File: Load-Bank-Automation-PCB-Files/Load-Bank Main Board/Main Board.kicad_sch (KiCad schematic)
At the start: 4 parts

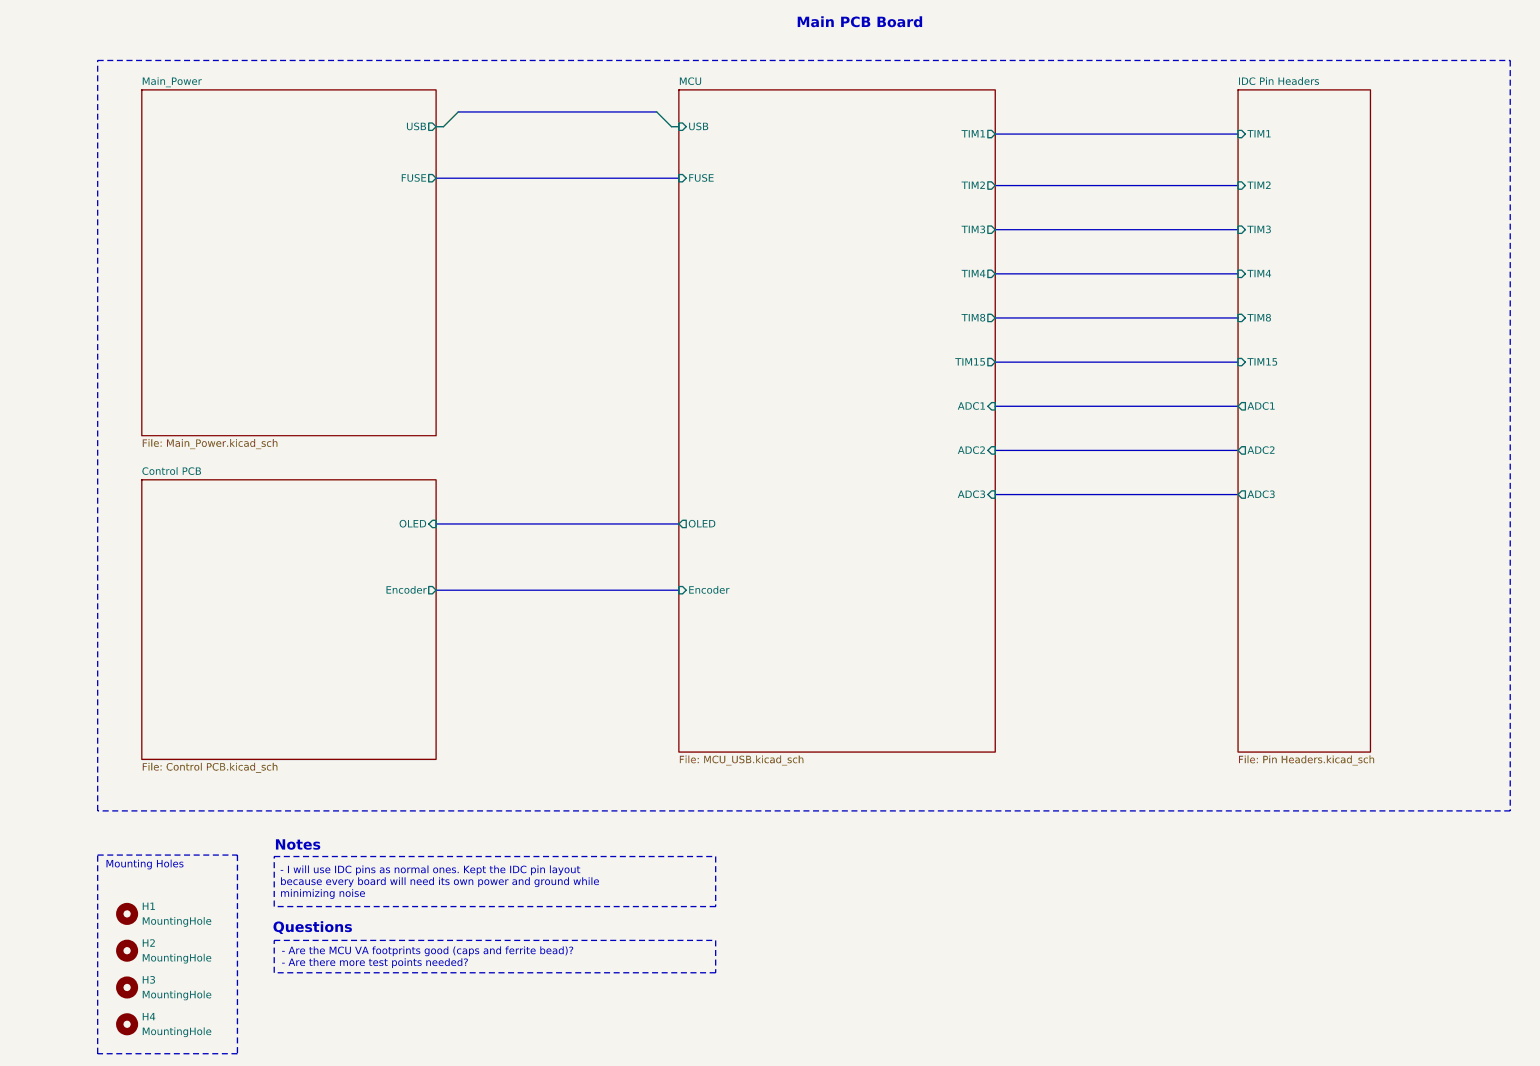
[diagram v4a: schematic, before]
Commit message: Schematic complete and  ready for review
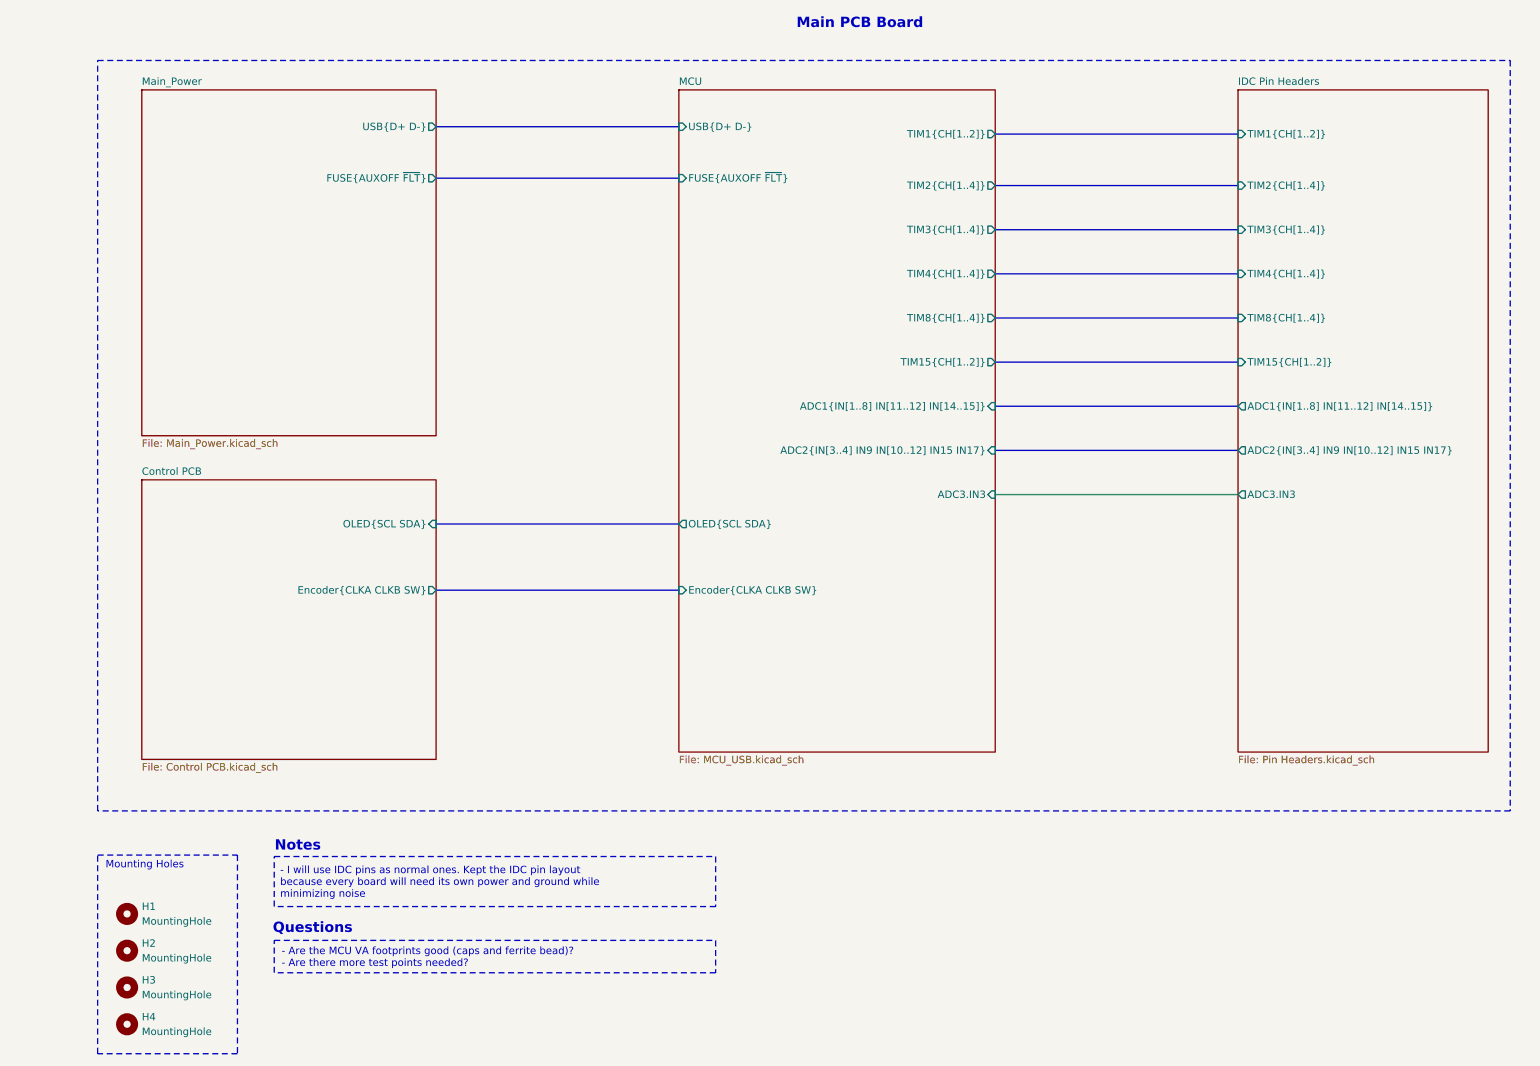
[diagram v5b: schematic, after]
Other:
- sheet Control PCB ports: added Encoder{CLKA CLKB SW}, OLED{SCL SDA}; removed Encoder, OLED
- sheet IDC Pin Headers ports: added ADC1{IN[1..8] IN[11..12] IN[14..15]}, ADC2{IN[3..4] IN9 IN[10..12] IN15 IN17}, ADC3.IN3, TIM15{CH[1..2]}, TIM1{CH[1..2]}, TIM2{CH[1..4]}, TIM3{CH[1..4]}, TIM4{CH[1..4]}, TIM8{CH[1..4]}; removed ADC1, ADC2, ADC3, TIM1, TIM15, TIM2, TIM3, TIM4, TIM8
- sheet MCU ports: added ADC1{IN[1..8] IN[11..12] IN[14..15]}, ADC2{IN[3..4] IN9 IN[10..12] IN15 IN17}, ADC3.IN3, Encoder{CLKA CLKB SW}, FUSE{AUXOFF ~{FLT}}, OLED{SCL SDA}, TIM15{CH[1..2]}, TIM1{CH[1..2]}, TIM2{CH[1..4]}, TIM3{CH[1..4]}, TIM4{CH[1..4]}, TIM8{CH[1..4]}, USB{D+ D-}; removed ADC1, ADC2, ADC3, Encoder, FUSE, OLED, TIM1, TIM15, TIM2, TIM3, TIM4, TIM8, USB
- sheet Main_Power ports: added FUSE{AUXOFF ~{FLT}}, USB{D+ D-}; removed FUSE, USB
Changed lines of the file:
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@@
-		)
-	)
-	(bus_entry
-		(at 125.73 31.75)
-		(size 2.54 2.54)
-		(stroke
-			(width 0)
-			(type default)
-		)
-	)
-	(bus_entry
-		(at 91.44 31.75)
-		(size -2.54 2.54)
-		(stroke
-			(width 0)
-			(type default)
 		)
 	)
@@
 	(bus
 		(pts
+			(xy 87.63 114.3) (xy 129.54 114.3)
+		)
+		(stroke
+			(width 0)
+			(type default)
+		)
+	)
+	(bus
+		(pts
+			(xy 184.15 82.55) (xy 226.06 82.55)
+		)
+		(stroke
+			(width 0)
+			(type default)
+		)
+	)
+	(wire
+		(pts
 			(xy 184.15 97.79) (xy 226.06 97.79)
 		)
@@
 	(bus
 		(pts
-			(xy 87.63 114.3) (xy 129.54 114.3)
-		)
-		(stroke
-			(width 0)
-			(type default)
-		)
-	)
-	(bus
-		(pts
-			(xy 184.15 82.55) (xy 226.06 82.55)
-		)
-		(stroke
-			(width 0)
-			(type default)
-		)
-	)
-	(bus
-		(pts
 			(xy 184.15 67.31) (xy 226.06 67.31)
 		)
@@
 		)
 	)
-	(wire
-		(pts
-			(xy 128.27 34.29) (xy 129.54 34.29)
+	(bus
+		(pts
+			(xy 87.63 34.29) (xy 129.54 34.29)
 		)
 		(stroke
@@
 		)
 	)
-	(wire
-		(pts
-			(xy 87.63 34.29) (xy 88.9 34.29)
-		)
-		(stroke
-			(width 0)
-			(type default)
-		)
-	)
 	(bus
 		(pts
@@
 		(pts
 			(xy 184.15 35.56) (xy 226.06 35.56)
-		)
-		(stroke
-			(width 0)
-			(type default)
-		)
-	)
-	(bus
-		(pts
-			(xy 91.44 31.75) (xy 125.73 31.75)
 		)
 		(stroke
@@
 	(sheet
 		(at 226.06 27.94)
-		(size 22.86 114.3)
+		(size 43.18 114.3)
 		(exclude_from_sim no)
 		(in_bom yes)
@@
 			)
 		)
-		(pin "TIM1" input
+		(pin "TIM1{CH[1..2]}" input
 			(at 226.06 35.56 180)
 			(effects
@@
 			)
 		)
-		(pin "TIM4" input
+		(pin "TIM4{CH[1..4]}" input
 			(at 226.06 59.69 180)
 			(effects
@@
 			)
 		)
-		(pin "ADC3" output
+		(pin "ADC3.IN3" output
 			(at 226.06 97.79 180)
 			(effects
@@
 			)
 		)
-		(pin "ADC2" output
+		(pin "ADC2{IN[3..4] IN9 IN[10..12] IN15 IN17}" output
 			(at 226.06 90.17 180)
 			(effects
@@
 			)
 		)
-		(pin "ADC1" output
+		(pin "ADC1{IN[1..8] IN[11..12] IN[14..15]}" output
 			(at 226.06 82.55 180)
 			(effects
@@
 			)
 		)
-		(pin "TIM8" input
+		(pin "TIM8{CH[1..4]}" input
 			(at 226.06 67.31 180)
 			(effects
@@
 			)
 		)
-		(pin "TIM2" input
+		(pin "TIM2{CH[1..4]}" input
 			(at 226.06 44.45 180)
 			(effects
@@
 			)
 		)
-		(pin "TIM15" input
+		(pin "TIM15{CH[1..2]}" input
 			(at 226.06 74.93 180)
 			(effects
@@
 			)
 		)
-		(pin "TIM3" input
+		(pin "TIM3{CH[1..4]}" input
 			(at 226.06 52.07 180)
 			(effects
@@
 			)
 		)
-		(pin "OLED" input
+		(pin "OLED{SCL SDA}" input
 			(at 87.63 102.87 0)
 			(effects
@@
 			)
 		)
-		(pin "Encoder" output
+		(pin "Encoder{CLKA CLKB SW}" output
 			(at 87.63 114.3 0)
 			(effects
@@
 			)
 		)
-		(pin "Encoder" input
+		(pin "Encoder{CLKA CLKB SW}" input
 			(at 129.54 114.3 180)
 			(effects
@@
 			)
 		)
-		(pin "TIM1" output
+		(pin "TIM1{CH[1..2]}" output
 			(at 184.15 35.56 0)
 			(effects
@@
 			)
 		)
-		(pin "USB" input
+		(pin "USB{D+ D-}" input
 			(at 129.54 34.29 180)
 			(effects
@@
 			)
 		)
-		(pin "TIM15" output
+		(pin "TIM15{CH[1..2]}" output
 			(at 184.15 74.93 0)
 			(effects
@@
 			)
 		)
-		(pin "ADC1" input
+		(pin "ADC1{IN[1..8] IN[11..12] IN[14..15]}" input
 			(at 184.15 82.55 0)
 			(effects
@@
 			)
 		)
-		(pin "ADC2" input
+		(pin "ADC2{IN[3..4] IN9 IN[10..12] IN15 IN17}" input
 			(at 184.15 90.17 0)
 			(effects
@@
 			)
 		)
-		(pin "TIM2" output
+		(pin "TIM2{CH[1..4]}" output
 			(at 184.15 44.45 0)
 			(effects
@@
 			)
 		)
-		(pin "TIM8" output
+		(pin "TIM8{CH[1..4]}" output
 			(at 184.15 67.31 0)
 			(effects
@@
 			)
 		)
-		(pin "TIM3" output
+		(pin "TIM3{CH[1..4]}" output
 			(at 184.15 52.07 0)
 			(effects
@@
 			)
 		)
-		(pin "OLED" output
+		(pin "ADC3.IN3" input
+			(at 184.15 97.79 0)
+			(effects
+				(font
+					(size 1.27 1.27)
+				)
+				(justify right)
+			)
+		)
+		(pin "TIM4{CH[1..4]}" output
+			(at 184.15 59.69 0)
+			(effects
+				(font
+					(size 1.27 1.27)
+				)
+				(justify right)
+			)
+		)
+		(pin "FUSE{AUXOFF ~{FLT}}" input
+			(at 129.54 43.18 180)
+			(effects
+				(font
+					(size 1.27 1.27)
+				)
+				(justify left)
+			)
+		)
+		(pin "OLED{SCL SDA}" output
 			(at 129.54 102.87 180)
-			(effects
-				(font
-					(size 1.27 1.27)
-				)
-				(justify left)
-			)
-		)
-		(pin "ADC3" input
-			(at 184.15 97.79 0)
-			(effects
-				(font
-					(size 1.27 1.27)
-				)
-				(justify right)
-			)
-		)
-		(pin "TIM4" output
-			(at 184.15 59.69 0)
-			(effects
-				(font
-					(size 1.27 1.27)
-				)
-				(justify right)
-			)
-		)
-		(pin "FUSE" input
-			(at 129.54 43.18 180)
 			(effects
 				(font
@@
 			)
 		)
-		(pin "USB" output
+		(pin "USB{D+ D-}" output
 			(at 87.63 34.29 0)
 			(effects
@@
 			)
 		)
-		(pin "FUSE" output
+		(pin "FUSE{AUXOFF ~{FLT}}" output
 			(at 87.63 43.18 0)
 			(effects

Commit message: A
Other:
- sheet MCU ports: added none; removed FUSE{AUXOFF ~{FLT}}
- sheet Main_Power ports: added none; removed FUSE{AUXOFF ~{FLT}}
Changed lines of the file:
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@@
-	(bus
-		(pts
-			(xy 87.63 43.18) (xy 129.54 43.18)
-		)
-		(stroke
-			(width 0)
-			(type default)
-		)
-	)
 	(bus
 		(pts
@@
 			)
 		)
-		(pin "FUSE{AUXOFF ~{FLT}}" input
-			(at 129.54 43.18 180)
-			(effects
-				(font
-					(size 1.27 1.27)
-				)
-				(justify left)
-			)
-		)
 		(pin "OLED{SCL SDA}" output
 			(at 129.54 102.87 180)
@@
 			(effects
 				(font
-					(size 1.27 1.27)
-				)
-				(justify right)
-			)
-		)
-		(pin "FUSE{AUXOFF ~{FLT}}" output
-			(at 87.63 43.18 0)
-			(effects
-				(font

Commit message: A
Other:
- note added: "- eFuse caps can be reconfigured to attain a more reliable output capacitance (some are rated for 25V, expensive caps, big tolarnaces of 20%)"
- note removed: "- I will use IDC pins as normal ones. Kept the IDC pin layout because every board will need its own power and ground while minimizing noise"
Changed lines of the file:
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@@
 		)
 	)
-	(text "- I will use IDC pins as normal ones. Kept the IDC pin layout\nbecause every board will need its own power and ground while\nminimizing noise"
+	(text "- eFuse caps can be reconfigured to attain a more reliable output \ncapacitance (some are rated for 25V, expensive caps, big tolarnaces \nof 20%)\n"
 		(exclude_from_sim no)
 		(at 60.706 164.846 0)
